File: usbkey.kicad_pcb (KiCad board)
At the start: 2 copper layers, 0 parts

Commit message: Actually have a design.
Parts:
- added C1: 1uF, Capacitors_SMD:C_0402, B.Cu at (34.6, 26.1)
- added C2: 1uF, Capacitors_SMD:C_0402, B.Cu at (41.0, 27.2)
- added C3: 47uF, Capacitors_SMD:C_0402, B.Cu at (36.9, 27.2)
- added D1: LED, LEDs:LED_0402, B.Cu at (32.9, 19.4)
- added D2: LED, LEDs:LED_0402, B.Cu at (31.2, 30.8)
- added P1: USART0, Pin_Headers:Pin_Header_Angled_1x04, F.Cu at (41.9, -4.44)
- added P2: DEBUG, Pin_Headers:Pin_Header_Angled_1x04, F.Cu at (59.6, -4.12)
- added P3: USB_B, Connect:USB_B, F.Cu at (23.4, 25.1)
- added R1: 15, Resistors_SMD:R_0402, B.Cu at (33.3, 17.6)
- added R2: 15, Resistors_SMD:R_0402, B.Cu at (33.0, 30.6)
- added R3: 15, Resistors_SMD:R_0402, B.Cu at (34.3, 23.5)
- added R4: 15, Resistors_SMD:R_0402, B.Cu at (34.3, 21.9)
- added REF**: SSOP-20_4.4x6.5mm_Pitch0.65mm, Housings_SSOP:SSOP-20_4.4x6.5mm_Pitch0.65mm, F.Cu at (52.5, 22.9)
- added REF**: QFN-32-1EP_5x5mm_Pitch0.5mm, Housings_DFN_QFN:QFN-32-1EP_5x5mm_Pitch0.5mm, B.Cu at (51.8, 15.8)
- added REF**: QFN-28-1EP_4x4mm_Pitch0.4mm, Housings_DFN_QFN:QFN-28-1EP_4x4mm_Pitch0.4mm, F.Cu at (55.7, 53.0)
- added REF**: SOT-23-6_Handsoldering, TO_SOT_Packages_SMD:SOT-23-6_Handsoldering, F.Cu at (22.9, 42.0)
- added REF**: SOT-23, TO_SOT_Packages_SMD:SOT-23, B.Cu at (59.7, 21.5)
- added REF**: SOT-23_Handsoldering, TO_SOT_Packages_SMD:SOT-23_Handsoldering, F.Cu at (30.5, 42.0)
- added REF**: SC-70, TO_SOT_Packages_SMD:SC-70, F.Cu at (58.8, 15.2)
- added REF**: SOT-323, TO_SOT_Packages_SMD:SOT-323, F.Cu at (58.7, 18.2)
- added U1: EFM32HG309, Housings_DFN_QFN:QFN-24-1EP_5x5mm_Pitch0.65mm, B.Cu at (39.0, 22.6)
- added W1: CAP0, Measurement_Points:Test_Point_2Pads, F.Cu at (28.1, 19.4)
- added W2: CAP1, Measurement_Points:Test_Point_2Pads, F.Cu at (27.9, 27.6)
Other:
- net class Default: clearance 0.2 -> 0.127; trace_width 0.25 -> 0.127
- rule trace_clearance: 0.2 -> 0.127
- board text added: "Front - Debug Pads Bottom - IC"
- board text added: "UFQFPN32 - STM32F042x4 - STM32L442KC 24-QFN - Silicon Labs - EFM32HG308 - EFM32HG350 - NXP - MKL27Z32Vxx4"

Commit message: Cleaning up some parts.
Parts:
- removed REF**: SSOP-20_4.4x6.5mm_Pitch0.65mm, Housings_SSOP:SSOP-20_4.4x6.5mm_Pitch0.65mm
- removed REF**: QFN-32-1EP_5x5mm_Pitch0.5mm, Housings_DFN_QFN:QFN-32-1EP_5x5mm_Pitch0.5mm
- removed REF**: QFN-28-1EP_4x4mm_Pitch0.4mm, Housings_DFN_QFN:QFN-28-1EP_4x4mm_Pitch0.4mm
- removed REF**: SOT-23-6_Handsoldering, TO_SOT_Packages_SMD:SOT-23-6_Handsoldering
- removed REF**: SOT-23, TO_SOT_Packages_SMD:SOT-23
- removed REF**: SOT-23_Handsoldering, TO_SOT_Packages_SMD:SOT-23_Handsoldering
- removed REF**: SC-70, TO_SOT_Packages_SMD:SC-70
- removed REF**: SOT-323, TO_SOT_Packages_SMD:SOT-323

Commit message: Give all the nets names.
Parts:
- moved P3 25.5 mm to (21.4, -0.33)
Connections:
- net Net-(C1-Pad2) renamed /DEC
- net Net-(P1-Pad2) renamed /US0_RX
- net Net-(P1-Pad3) renamed /US0_TX
- net Net-(R1-Pad1) renamed /LED1
- net Net-(R2-Pad2) renamed /LED0
- net Net-(R3-Pad2) renamed /RUSB_D+
- net Net-(R4-Pad2) renamed /RUSB_D-
- net Net-(U1-Pad23) renamed /CAP1
- net Net-(U1-Pad24) renamed /CAP0
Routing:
- net +3V3: track 0.00 -> 15.2 mm
- net /CAP0: track 0.00 -> 3.35 mm
- net (no net): track 82.9 -> 85.1 mm, vias 0 -> 1
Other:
- net class Default: clearance 0.127 -> 0.1016; trace_width 0.127 -> 0.1016; via_drill 0.4 -> 0.3
- rule trace_clearance: 0.127 -> 0.1016

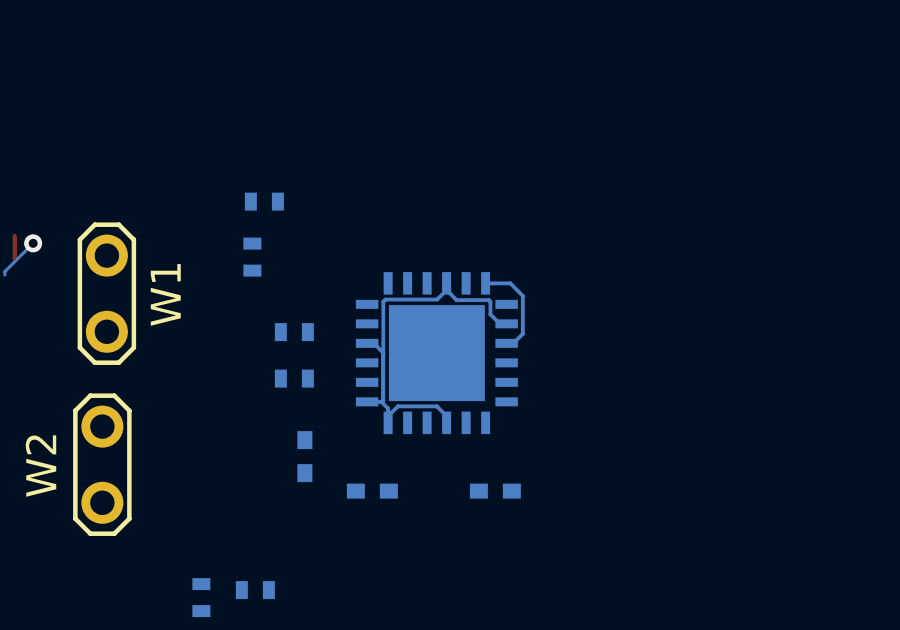
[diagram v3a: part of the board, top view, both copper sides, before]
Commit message: Playing with things.
ADC on one side, capacitive on the other.

Starting on USB PCB component.
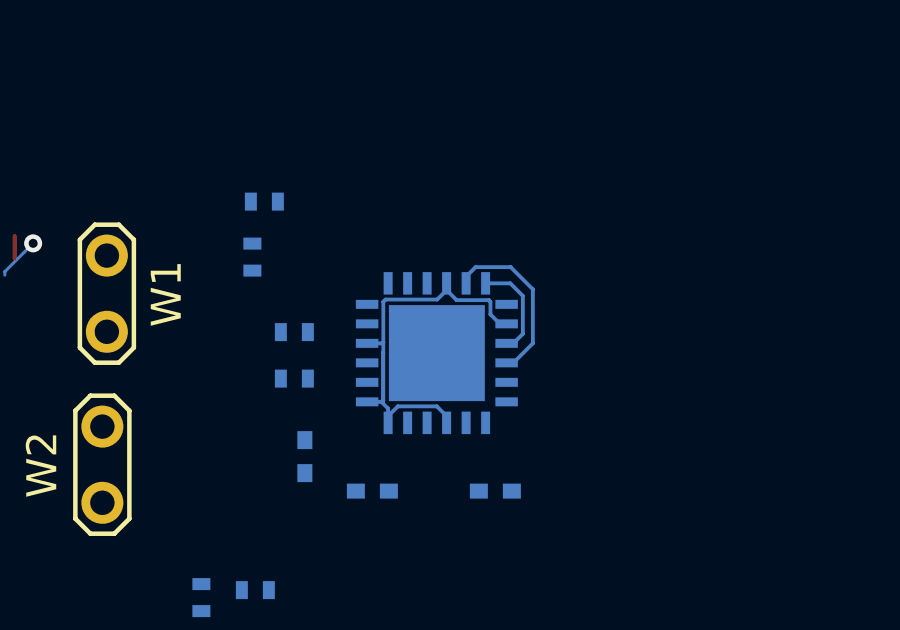
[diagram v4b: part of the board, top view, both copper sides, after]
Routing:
- net /CAP1: track 0.00 -> 5.83 mm
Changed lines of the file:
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@@
   (general
     (links 42)
-    (no_connects 36)
+    (no_connects 35)
     (area 0 0 0 0)
     (thickness 1.6)
     (drawings 46)
-    (tracks 53)
+    (tracks 62)
     (zones 0)
     (modules 15)
@@
   (segment (start 17 29) (end 29 29) (width 0.0254) (layer Dwgs.User) (net 0))
   (segment (start 17 18) (end 17 29) (width 0.0254) (layer Dwgs.User) (net 0))
+  (segment (start 37.265101 22.640101) (end 37.265101 22.3) (width 0.127) (layer B.Cu) (net 2))
+  (segment (start 37.265101 22.3) (end 37.265101 20.937717) (width 0.127) (layer B.Cu) (net 2))
+  (segment (start 36.725 22.325) (end 37.227 22.325) (width 0.127) (layer B.Cu) (net 2))
+  (segment (start 37.227 22.325) (end 37.252 22.3) (width 0.127) (layer B.Cu) (net 2))
+  (segment (start 37.252 22.3) (end 37.265101 22.3) (width 0.127) (layer B.Cu) (net 2))
   (segment (start 39.375 20.325) (end 39.375 20.55) (width 0.127) (layer B.Cu) (net 2))
   (segment (start 39.375 20.55) (end 39.709899 20.884899) (width 0.127) (layer B.Cu) (net 2))
@@
   (segment (start 41.15 21.675) (end 41.375 21.675) (width 0.127) (layer B.Cu) (net 2))
   (segment (start 40.834899 21.359899) (end 41.15 21.675) (width 0.127) (layer B.Cu) (net 2))
-  (segment (start 37.265101 22.640101) (end 37.265101 20.937717) (width 0.127) (layer B.Cu) (net 2))
   (segment (start 37.265101 20.937717) (end 37.337717 20.865101) (width 0.127) (layer B.Cu) (net 2))
   (segment (start 37.337717 20.865101) (end 39.059899 20.865101) (width 0.127) (layer B.Cu) (net 2))
@@
   (segment (start 37.227 24.275) (end 37.265101 24.236899) (width 0.127) (layer B.Cu) (net 2))
   (segment (start 37.265101 24.236899) (end 37.265101 22.640101) (width 0.127) (layer B.Cu) (net 2))
-  (segment (start 37.265101 22.640101) (end 36.95 22.325) (width 0.127) (layer B.Cu) (net 2))
   (segment (start 36.95 22.325) (end 36.725 22.325) (width 0.127) (layer B.Cu) (net 2))
   (segment (start 37.227 24.275) (end 36.725 24.275) (width 0.127) (layer B.Cu) (net 2))
@@
   (segment (start 39.375 24.75) (end 39.375 24.975) (width 0.127) (layer B.Cu) (net 2))
   (segment (start 37.214301 24.220043) (end 37.214301 22.589301) (width 0.0254) (layer B.Cu) (net 2))
-  (segment (start 37.214301 22.589301) (end 36.95 22.325) (width 0.0254) (layer B.Cu) (net 2))
   (segment (start 37.425 24.975) (end 37.425 24.75) (width 0.0254) (layer B.Cu) (net 2))
   (segment (start 40.675 20.325) (end 41.497182 20.325) (width 0.127) (layer B.Cu) (net 21))
@@
   (segment (start 41.915101 22.009899) (end 41.6 22.325) (width 0.127) (layer B.Cu) (net 21))
   (segment (start 41.6 22.325) (end 41.375 22.325) (width 0.127) (layer B.Cu) (net 21))
+  (segment (start 42.25 20.525) (end 41.509899 19.784899) (width 0.127) (layer B.Cu) (net 22))
+  (segment (start 41.509899 19.784899) (end 40.340101 19.784899) (width 0.127) (layer B.Cu) (net 22))
+  (segment (start 40.340101 19.784899) (end 40.025 20.1) (width 0.127) (layer B.Cu) (net 22))
+  (segment (start 40.025 20.1) (end 40.025 20.325) (width 0.127) (layer B.Cu) (net 22))
+  (segment (start 42.25 22.325) (end 42.25 20.525) (width 0.127) (layer B.Cu) (net 22))
+  (segment (start 41.375 22.975) (end 41.6 22.975) (width 0.127) (layer B.Cu) (net 22))
+  (segment (start 41.6 22.975) (end 42.25 22.325) (width 0.127) (layer B.Cu) (net 22))
 )

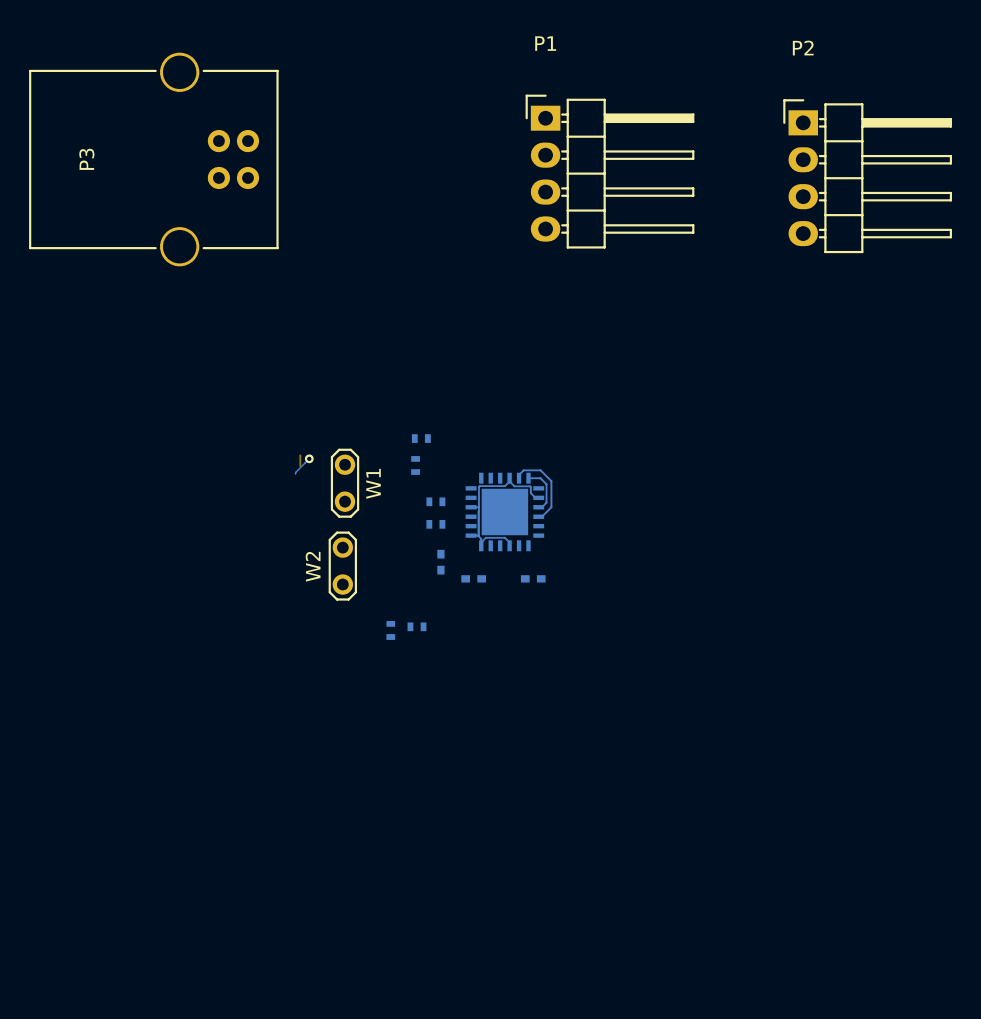
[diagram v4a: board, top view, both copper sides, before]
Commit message: Working on a 2-layer 0.4mm PCB design.
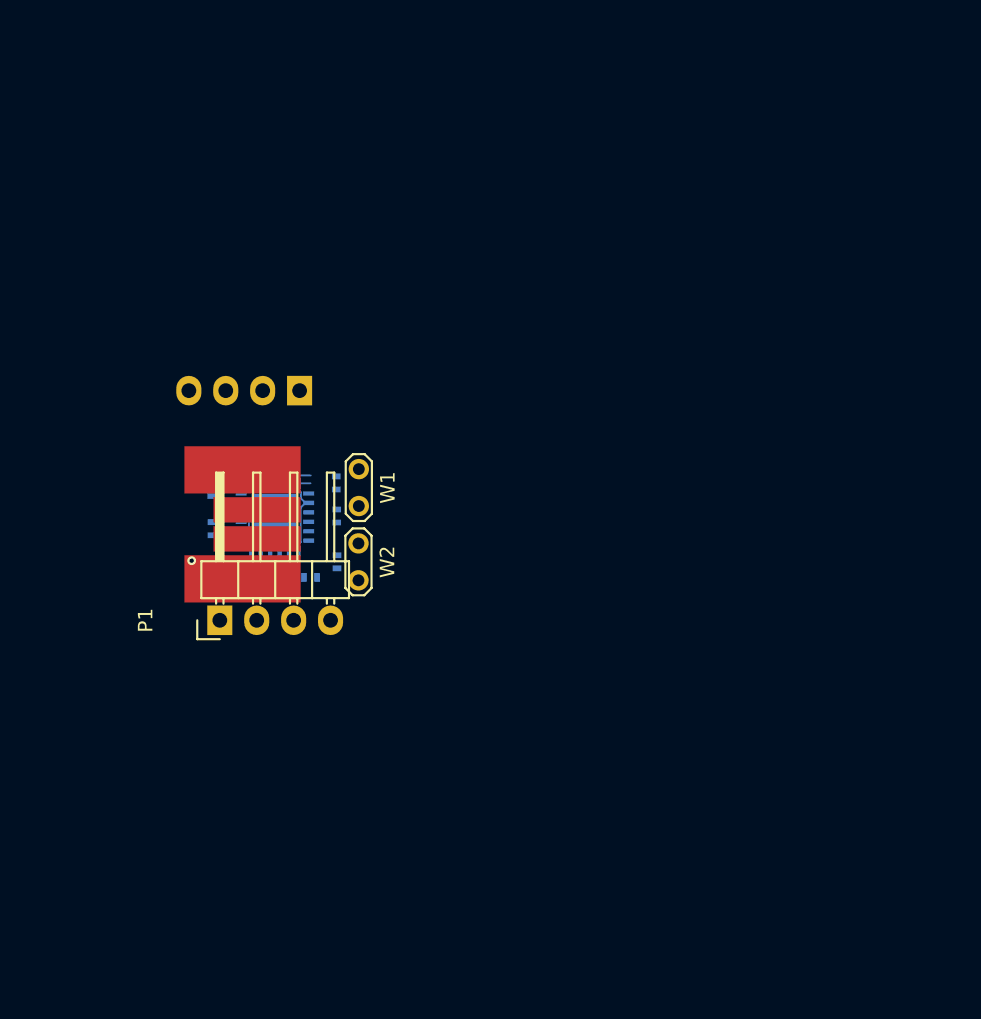
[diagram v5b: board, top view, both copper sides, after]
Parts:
- P2: moved to B.Cu
- P3: footprint Connect:USB_B -> usb-pcb:USB-PCB
- moved P1 41.2 mm to (19.4, 30.1), turned to 90 degrees
- moved P2 39.2 mm to (24.9, 14.3), turned to 90 degrees
- moved P3 29.7 mm to (17.0, 29.0), turned to 0 degrees
- moved C2 17.7 mm to (23.3, 27.2), turned to 180 degrees
- moved C3 16.1 mm to (20.8, 27.1)
- moved C1 15.8 mm to (18.8, 26.6)
- moved U1 15.8 mm to (23.2, 23.0)
- moved R4 15.4 mm to (18.9, 21.1), turned to 90 degrees
- moved R3 15.4 mm to (18.9, 23.8), turned to 90 degrees
- moved R2 8.08 mm to (25.7, 27.1), turned to 180 degrees
- moved R1 7.89 mm to (27.5, 22.9), turned to 90 degrees
- moved D2 6.00 mm to (27.5, 26.1)
- moved D1 5.58 mm to (27.4, 20.6), turned to 90 degrees
- moved W2 3.03 mm to (29.0, 24.8), turned to 270 degrees
- moved W1 1.00 mm to (29.0, 19.7)
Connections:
- U1 pad 23: /CAP1 -> /CAP0B
- U1 pad 24: /CAP0 -> /CAP1B
- U1 pad 3: /CAP0 -> /CAP0A
- U1 pad 4: /CAP1 -> /CAP1A
- W1 pad 1: GND -> /CAP0B
- W1 pad 2: /CAP0 -> /CAP0A
- W2 pad 1: GND -> /CAP1B
- W2 pad 2: /CAP1 -> /CAP1A
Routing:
- net /CAP1: track 5.83 -> 0.00 mm
- net /CAP0: track 3.35 -> 0.00 mm
- net (no net): track 85.1 -> 82.9 mm, vias 1 -> 0
- net /CAP0B: track 0.00 -> 1.84 mm
- net +3V3: track 14.9 -> 13.5 mm
- net /CAP1B: track 0.00 -> 0.82 mm
- net /USB_5V: track 0.00 -> 0.45 mm, vias 0 -> 1
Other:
- board text removed: "D+"
- board text removed: "D-"
- board text removed: "GND"
- board text removed: "VCC"

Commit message: Temp commit.
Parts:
- moved P2 8.52 mm to (18.0, 19.2), turned to 270 degrees
- moved P1 7.57 mm to (27.0, 30.2), turned to 270 degrees
- moved C1 2.99 mm to (21.8, 27.2), turned to 180 degrees
- moved R2 2.15 mm to (26.9, 25.4), turned to 90 degrees
- moved C3 1.53 mm to (19.3, 27.2)
- moved D2 1.46 mm to (26.6, 27.2), turned to 180 degrees
- moved C2 0.88 mm to (24.2, 27.2), turned to 0 degrees
- moved R3 0.79 mm to (19.1, 23.0), turned to 0 degrees
- moved R1 0.75 mm to (27.3, 22.2)
- moved D1 0.62 mm to (27.3, 20.1)
- moved U1 0.47 mm to (23.1, 23.4)
- moved R4 0.18 mm to (19.1, 21.1), turned to 0 degrees
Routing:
- net GND: track 0.00 -> 22.8 mm, vias 0 -> 1
- net /US0_TX: track 0.00 -> 8.28 mm
- net /US0_RX: track 0.00 -> 7.57 mm
- net /USB_D-: track 0.00 -> 6.84 mm, vias 0 -> 1
- net /CAP1A: track 0.22 -> 6.40 mm
- net /CAP1B: track 0.82 -> 6.55 mm
- net +3V3: track 13.5 -> 18.4 mm
- net /USB_D+: track 0.00 -> 4.32 mm, vias 0 -> 1
- net /CAP0A: track 0.22 -> 4.25 mm, vias 0 -> 1
- net /USB_5V: track 0.45 -> 4.46 mm
- net /LED0: track 0.00 -> 3.83 mm
- net /CAP0B: track 1.84 -> 5.67 mm
- net /DEC: track 0.22 -> 3.76 mm
- net /LED1: track 0.00 -> 2.24 mm
- net /RUSB_D-: track 0.00 -> 1.73 mm
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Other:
- net class Default: clearance 0.1016 -> 0.102; trace_width 0.1016 -> 0.102
- rule trace_clearance: 0.1016 -> 0.102

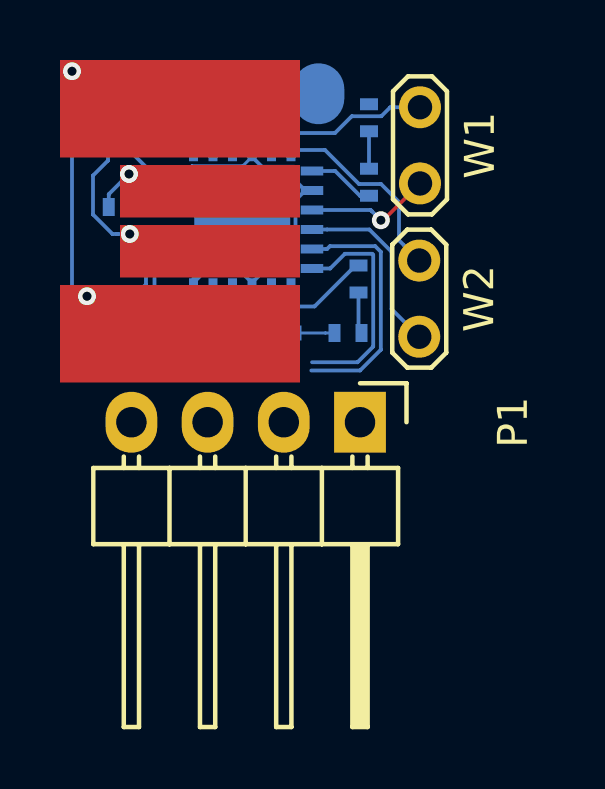
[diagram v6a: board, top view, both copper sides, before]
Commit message: Lots of modifications.
Trying to make 5mil/5mil pass.
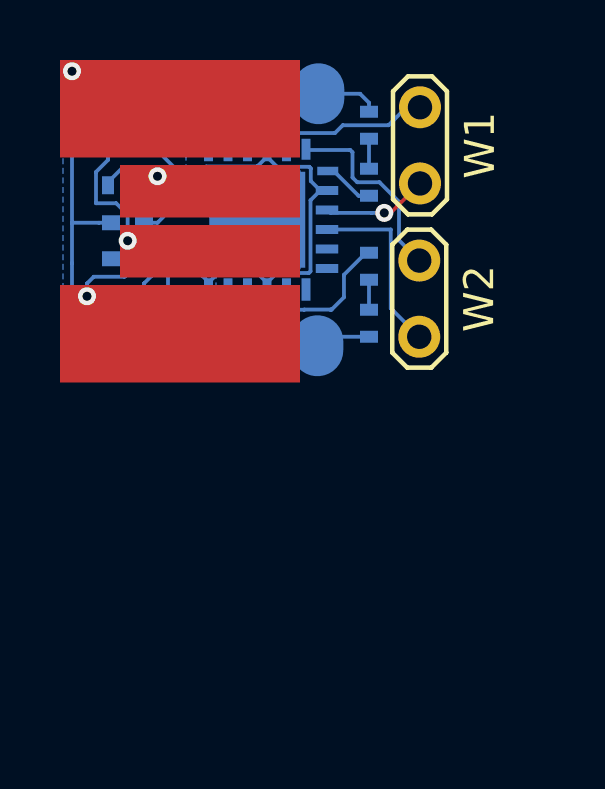
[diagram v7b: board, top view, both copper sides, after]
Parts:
- P1: moved to B.Cu
- moved P1 9.39 mm to (18.0, 27.6)
- moved C2 6.17 mm to (19.2, 23.6), turned to 180 degrees
- moved C1 2.81 mm to (19.2, 25.9), turned to 0 degrees
- moved C3 2.48 mm to (19.2, 24.8), turned to 180 degrees
- moved D2 0.77 mm to (27.3, 26.9), turned to 270 degrees
- moved R3 0.73 mm to (19.1, 22.3)
- moved R2 0.55 mm to (27.3, 25.0)
- moved U1 0.50 mm to (23.6, 23.4)
- moved D1 0.25 mm to (27.3, 20.3)
- moved R4 0.05 mm to (19.1, 21.0)
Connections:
- D1 pad 2: GND -> +3V3
- D2 pad 2: GND -> +3V3
- P1 pad 2: /US0_RX -> /LEU0_RX
- P1 pad 3: /US0_TX -> /LEU0_TX
- P2 pad 2: /DBG_SWDIO -> /DBG_SWCLK
- P2 pad 3: /DBG_SWCLK -> /DBG_SWDIO
- P3 pad 2: /USB_D+ -> /USB_D-
- P3 pad 3: /USB_D- -> /USB_D+
- R3 pad 1: /USB_D+ -> /USB_D-
- R3 pad 2: /RUSB_D+ -> /RUSB_D-
- R4 pad 1: /USB_D- -> /USB_D+
- R4 pad 2: /RUSB_D- -> /RUSB_D+
- U1 pad 10: Net-(U1-Pad10) -> /LEU0_TX
- U1 pad 11: Net-(U1-Pad11) -> /LEU0_RX
- U1 pad 17: /RUSB_D+ -> /RUSB_D-
- U1 pad 18: /RUSB_D- -> /RUSB_D+
- U1 pad 5: /US0_TX -> Net-(U1-Pad5)
- U1 pad 6: /US0_RX -> Net-(U1-Pad6)
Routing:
- net (no net): track 82.9 -> 0.00 mm
- net +3V3: track 18.4 -> 27.5 mm
- net /US0_TX: track 8.28 -> 0.00 mm
- net /US0_RX: track 7.57 -> 0.00 mm
- net /LEU0_RX: track 0.00 -> 3.55 mm
- net /DBG_SWCLK: track 0.00 -> 3.03 mm
- net /USB_D-: track 6.84 -> 4.04 mm
- net /USB_D+: track 4.32 -> 6.99 mm
- net GND: track 22.8 -> 20.6 mm
- net /DBG_SWDIO: track 0.00 -> 2.07 mm
- net /LEU0_TX: track 0.00 -> 1.96 mm
- net /DEC: track 3.76 -> 2.47 mm
- net /LED0: track 3.83 -> 4.54 mm
- net /CAP0A: track 4.25 -> 3.56 mm
- net /RUSB_D+: track 1.51 -> 2.07 mm
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- added copper zone on B.Cu, net GND
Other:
- net class Default: clearance 0.102 -> 0.127; trace_width 0.102 -> 0.127
- rule trace_clearance: 0.102 -> 0.127
- rule trace_min: 0.0254 -> 0.127

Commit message: Lots more work.
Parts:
- moved P2 0.13 mm to (18.1, 19.4)
- moved P1 0.10 mm to (18.1, 27.6)
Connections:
- U1 pad 5: Net-(U1-Pad5) -> /LED0
- U1 pad 8: /LED0 -> Net-(U1-Pad8)
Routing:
- net GND: track 20.6 -> 39.4 mm, vias 1 -> 3
- net +3V3: track 27.5 -> 31.6 mm, vias 0 -> 2
- net /LED0: track 4.54 -> 1.45 mm
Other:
- board outline added: 12 x 11 mm
- rule trace_min: 0.127 -> 0.0254
